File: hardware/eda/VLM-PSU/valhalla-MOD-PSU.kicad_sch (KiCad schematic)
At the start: 58 parts, among them J1 MAINS, J2 DC, J3 BUS, J4 GPIO, J5 POWER, Q1 BTA08-600CW, Q10 IRF9Z34N, Q2 2N3904, Q3 2N3906, Q4 2N3906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

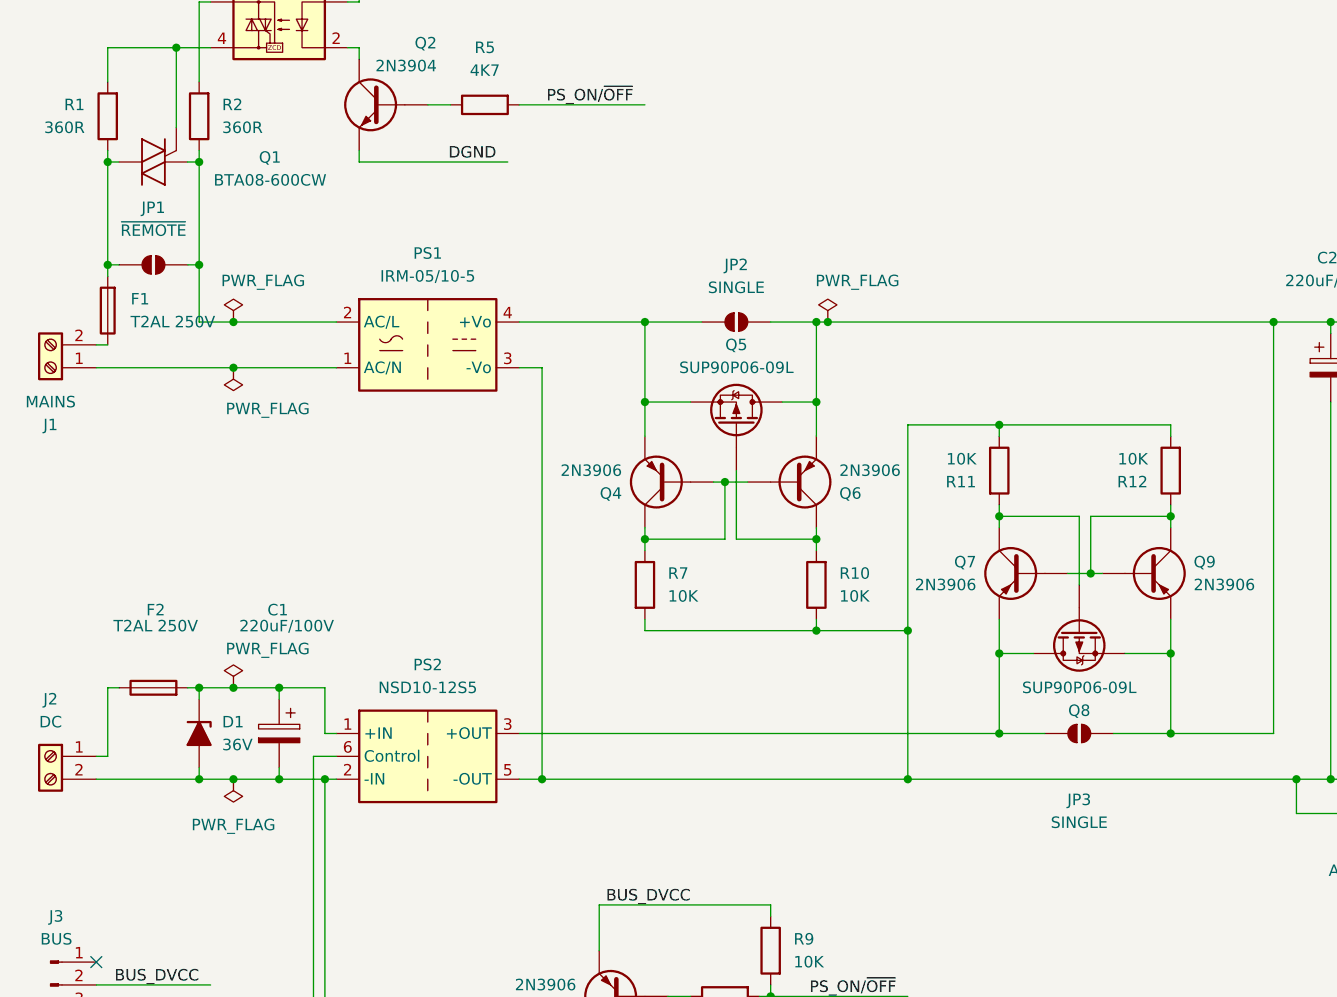
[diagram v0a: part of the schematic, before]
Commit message: UPDATE: tentative component placement for MOD-PSU
  - everything fits with room to spare
  - clearance/creepage for the mains section appears fine
  - zones/slots are next.
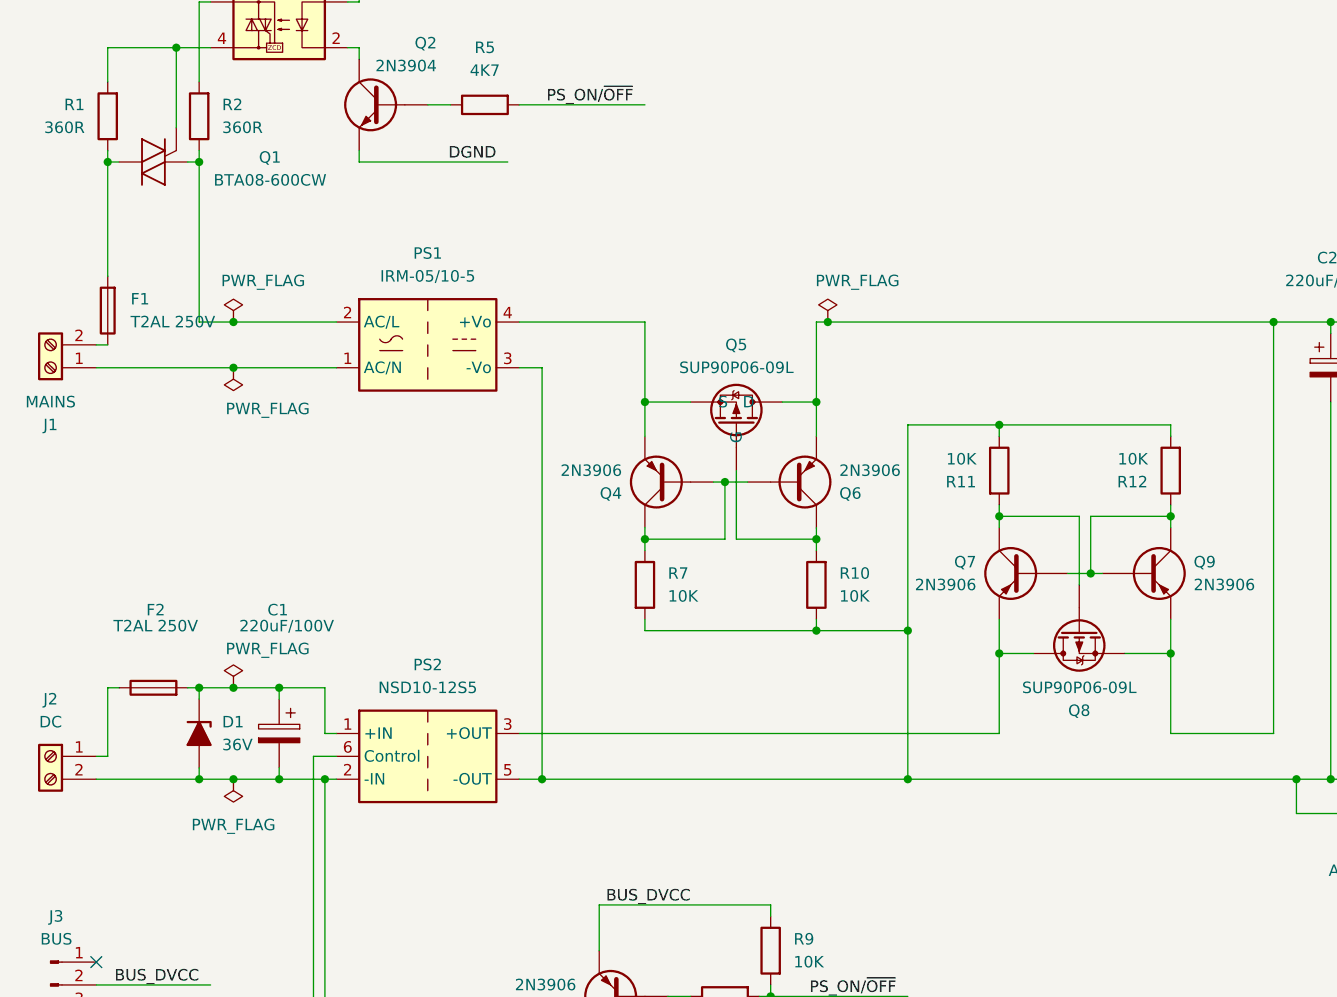
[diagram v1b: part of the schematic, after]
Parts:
- removed JP1: ~{REMOTE}, Jumper:SolderJumper-2_P1.3mm_Open_TrianglePad1.0x1.5mm, symbol Jumper:SolderJumper_2_Open
- removed JP2, JP3: SINGLE, Jumper:SolderJumper-2_P1.3mm_Open_TrianglePad1.0x1.5mm, symbol Jumper:SolderJumper_2_Open
- U3: footprint Package_TO_SOT_THT:TO-92_Inline -> Package_TO_SOT_THT:TO-92_Wide

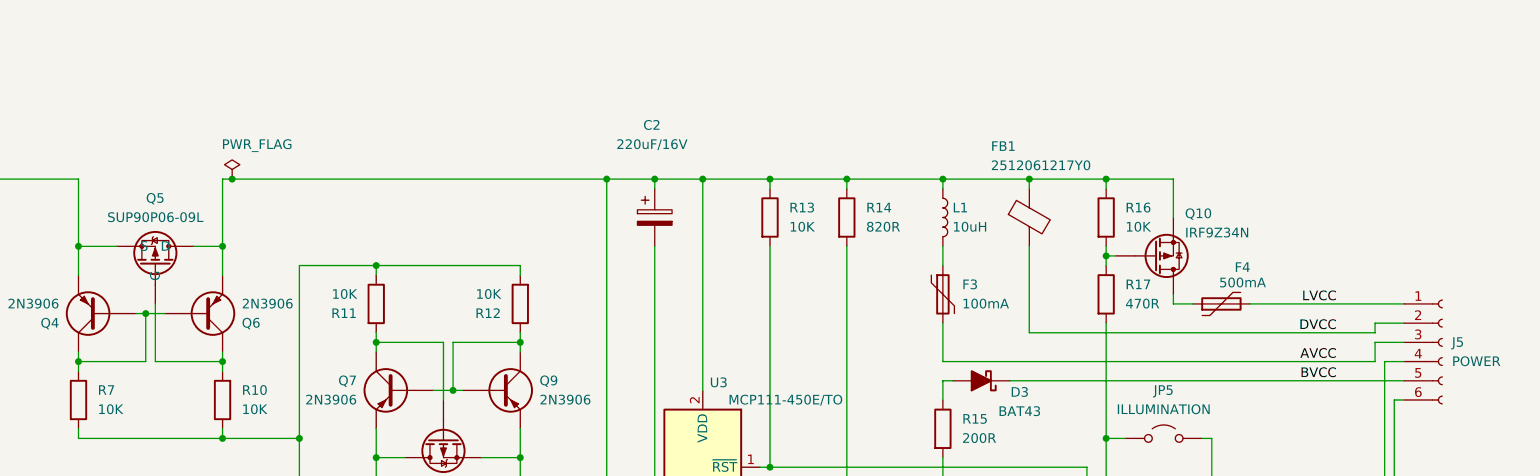
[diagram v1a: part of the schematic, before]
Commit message: UPDATE: progress on MOD-PSU layout
  - zones and slots done
  - heatsink pours and stiches done
  - routing is next.
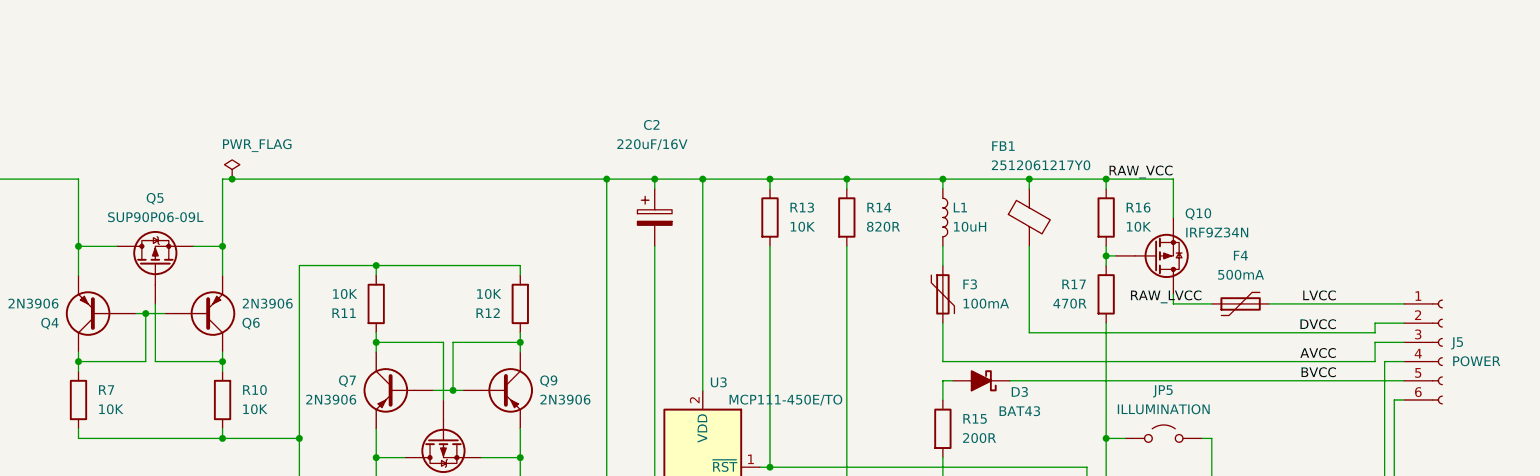
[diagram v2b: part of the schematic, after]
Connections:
- net RAW_LVCC: now reaches F4.1, Q10.2 (D)
- net RAW_VCC: now reaches C2.1, FB1.1, L1.1, Q10.3 (S), Q6.1 (E), Q8.3 (S), Q9.1 (E), R13.1, R14.1, R16.1, U3.2 (VDD)
- net RAW_VCC: now also Q5.3 (S); no longer Q5.2 (D)
- net at PS1.4 (+Vo), Q4.1 (E): now also Q5.2 (D); no longer Q5.3 (S)
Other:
- moved on the sheet: F4
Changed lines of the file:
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@@
 	(wire
 		(pts
-			(xy 228.6 78.74) (xy 231.14 78.74)
+			(xy 228.6 78.74) (xy 233.68 78.74)
 		)
 		(stroke
@@
 	(wire
 		(pts
-			(xy 238.76 78.74) (xy 259.08 78.74)
+			(xy 241.3 78.74) (xy 259.08 78.74)
 		)
 		(stroke
@@
 		)
 	)
+	(label "RAW_VCC"
+		(at 228.6 62.23 180)
+		(effects
+			(font
+				(size 1.27 1.27)
+			)
+			(justify right bottom)
+		)
+	)
 	(label "DGND"
 		(at 250.19 113.03 180)
@@
 		)
 	)
+	(label "RAW_LVCC"
+		(at 232.41 78.74 180)
+		(effects
+			(font
+				(size 1.27 1.27)
+			)
+			(justify right bottom)
+		)
+	)
 	(label "PS_ON{slash}~{OFF}"
 		(at 111.76 137.16 180)
@@
 		(fields_autoplaced yes)
 		(property "Reference" "R17"
-			(at 222.25 76.1999 0)
+			(at 217.17 76.1999 0)
 			(effects
 				(font
 					(size 1.27 1.27)
 				)
-				(justify left)
+				(justify right)
 			)
 		)
 		(property "Value" "470R"
-			(at 222.25 78.7399 0)
+			(at 217.17 78.7399 0)
 			(effects
 				(font
 					(size 1.27 1.27)
 				)
-				(justify left)
+				(justify right)
 			)
 		)
@@
 		(lib_name "IRF4905_2")
 		(lib_id "Transistor_FET:IRF4905")
-		(at 93.98 73.66 270)
-		(mirror x)
+		(at 93.98 73.66 90)
 		(unit 1)
 		(exclude_from_sim no)
@@
 		)
 		(property "Footprint" "Package_TO_SOT_THT:TO-220-3_Horizontal_TabDown"
-			(at 92.075 68.58 0)
+			(at 95.885 68.58 0)
 			(effects
 				(font
@@
 		)
 		(property "Datasheet" "http://www.infineon.com/dgdl/irf4905.pdf?fileId=5546d462533600a4015355e32165197c"
-			(at 90.17 68.58 0)
+			(at 97.79 68.58 0)
 			(effects
 				(font
@@
 	(symbol
 		(lib_id "Device:Polyfuse")
-		(at 234.95 78.74 90)
+		(at 237.49 78.74 90)
 		(unit 1)
 		(exclude_from_sim no)
@@
 		(on_board yes)
 		(dnp no)
+		(fields_autoplaced yes)
 		(property "Reference" "F4"
-			(at 237.744 73.914 90)
+			(at 237.49 72.39 90)
 			(effects
 				(font
@@
 		)
 		(property "Value" "500mA"
-			(at 237.744 75.946 90)
+			(at 237.49 74.93 90)
 			(effects
 				(font
@@
 		)
 		(property "Footprint" "Fuse:Fuse_BelFuse_0ZRE0005FF_L8.3mm_W3.8mm"
-			(at 240.03 77.47 0)
+			(at 242.57 77.47 0)
 			(effects
 				(font
@@
 		)
 		(property "Datasheet" "~"
-			(at 234.95 78.74 0)
+			(at 237.49 78.74 0)
 			(effects
 				(font
@@
 		)
 		(property "Description" "Resettable fuse, polymeric positive temperature coefficient"
-			(at 234.95 78.74 0)
+			(at 237.49 78.74 0)
 			(effects
 				(font

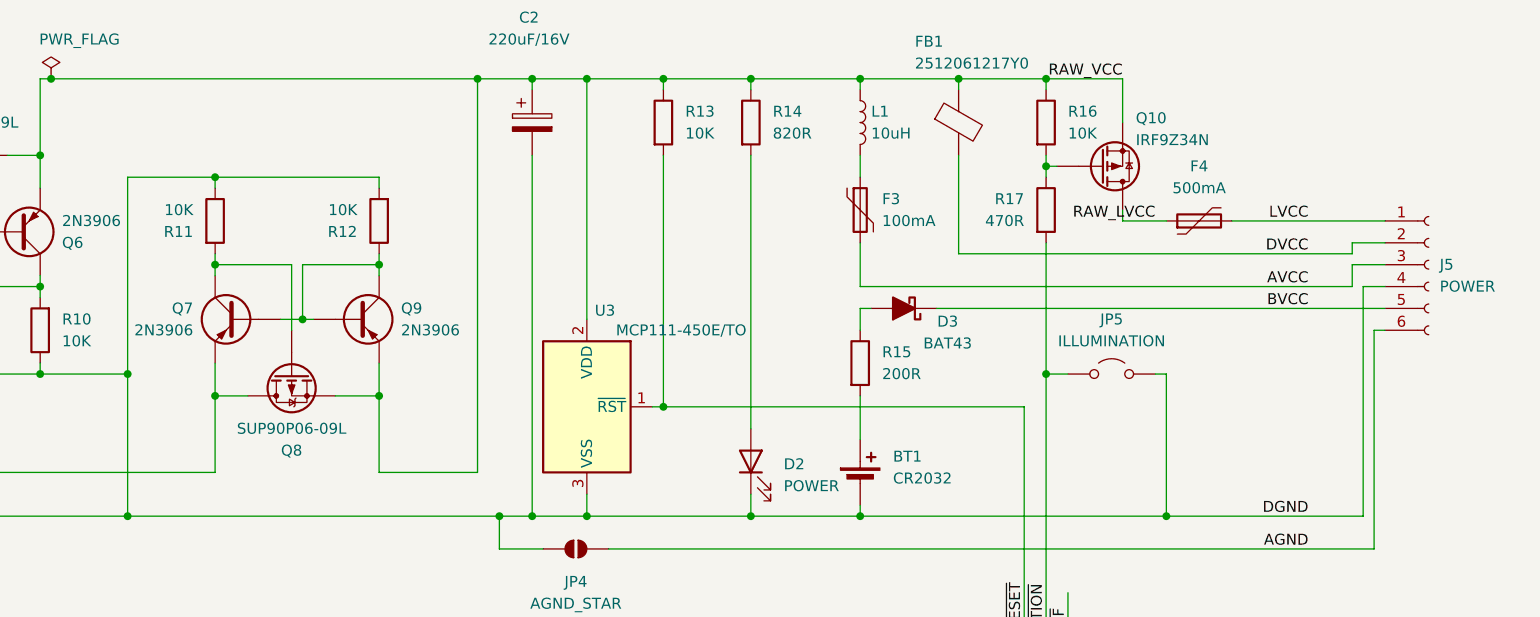
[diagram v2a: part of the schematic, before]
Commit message: UPDATE: progress on MOD-PSU
  - routing done, including copper heatsinks
  - silkscreen is last.
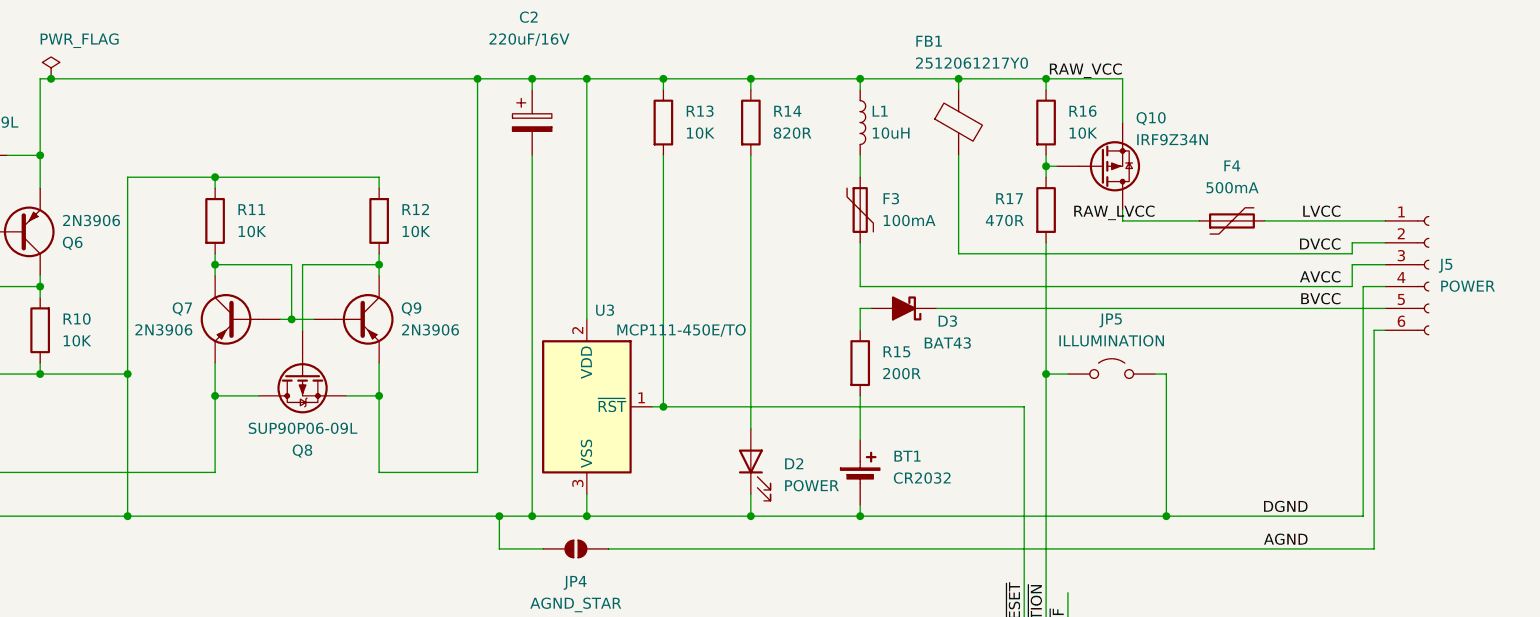
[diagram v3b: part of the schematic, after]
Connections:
- net at Q7.2 (B), Q9.2 (B): now also Q7.3 (C), R11.2; no longer Q9.3 (C), R12.1
- new net: Q8.1 (G), Q9.3 (C), R12.1
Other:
- moved on the sheet: F4, Q8
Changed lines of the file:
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@@
 	)
 	(junction
-		(at 133.35 90.17)
-		(diameter 0)
-		(color 0 0 0 0)
-	)
-	(junction
 		(at 219.71 62.23)
 		(diameter 0)
@@
 	)
 	(junction
+		(at 132.08 90.17)
+		(diameter 0)
+		(color 0 0 0 0)
+	)
+	(junction
 		(at 123.19 99.06)
 		(diameter 0)
@@
 	(wire
 		(pts
-			(xy 228.6 78.74) (xy 233.68 78.74)
+			(xy 228.6 78.74) (xy 237.49 78.74)
 		)
 		(stroke
@@
 	(wire
 		(pts
-			(xy 241.3 78.74) (xy 259.08 78.74)
+			(xy 245.11 78.74) (xy 259.08 78.74)
 		)
 		(stroke
@@
 	(wire
 		(pts
+			(xy 132.08 90.17) (xy 134.62 90.17)
+		)
+		(stroke
+			(width 0)
+			(type default)
+		)
+	)
+	(wire
+		(pts
 			(xy 219.71 72.39) (xy 220.98 72.39)
 		)
@@
 	(wire
 		(pts
+			(xy 133.35 83.82) (xy 133.35 91.44)
+		)
+		(stroke
+			(width 0)
+			(type default)
+		)
+	)
+	(wire
+		(pts
 			(xy 34.29 113.03) (xy 38.1 113.03)
 		)
@@
 	(wire
 		(pts
-			(xy 130.81 90.17) (xy 133.35 90.17)
+			(xy 130.81 90.17) (xy 132.08 90.17)
 		)
 		(stroke
@@
 	(wire
 		(pts
-			(xy 132.08 91.44) (xy 132.08 83.82)
-		)
-		(stroke
-			(width 0)
-			(type default)
-		)
-	)
-	(wire
-		(pts
 			(xy 24.13 31.75) (xy 31.75 31.75)
 		)
@@
 	(wire
 		(pts
-			(xy 137.16 99.06) (xy 142.24 99.06)
+			(xy 138.43 99.06) (xy 142.24 99.06)
 		)
 		(stroke
@@
 	(wire
 		(pts
+			(xy 132.08 83.82) (xy 132.08 90.17)
+		)
+		(stroke
+			(width 0)
+			(type default)
+		)
+	)
+	(wire
+		(pts
 			(xy 142.24 83.82) (xy 133.35 83.82)
 		)
@@
 	(wire
 		(pts
-			(xy 127 99.06) (xy 123.19 99.06)
+			(xy 128.27 99.06) (xy 123.19 99.06)
 		)
 		(stroke
@@
 	(wire
 		(pts
-			(xy 133.35 90.17) (xy 134.62 90.17)
-		)
-		(stroke
-			(width 0)
-			(type default)
-		)
-	)
-	(wire
-		(pts
 			(xy 62.23 156.21) (xy 46.99 156.21)
 		)
@@
 	(wire
 		(pts
-			(xy 133.35 83.82) (xy 133.35 90.17)
-		)
-		(stroke
-			(width 0)
-			(type default)
-		)
-	)
-	(wire
-		(pts
 			(xy 256.54 86.36) (xy 256.54 113.03)
 		)
@@
 	)
 	(label "AVCC"
-		(at 250.19 86.36 180)
+		(at 254 86.36 180)
 		(effects
 			(font
@@
 	)
 	(label "LVCC"
-		(at 250.19 78.74 180)
+		(at 254 78.74 180)
 		(effects
 			(font
@@
 	)
 	(label "DVCC"
-		(at 250.19 82.55 180)
+		(at 254 82.55 180)
 		(effects
 			(font
@@
 	)
 	(label "BVCC"
-		(at 250.19 88.9 180)
+		(at 254 88.9 180)
 		(effects
 			(font
@@
 		(length 2.54)
 		(shape round)
+		(at 228.6 78.74 180)
+		(fields_autoplaced yes)
+		(effects
+			(font
+				(size 1.27 1.27)
+			)
+			(justify right bottom)
+		)
+		(property "Netclass" "DCD_Power"
+			(at 229.2985 81.28 0)
+			(effects
+				(font
+					(size 1.27 1.27)
+					(italic yes)
+				)
+				(justify left)
+			)
+		)
+	)
+	(netclass_flag ""
+		(length 2.54)
+		(shape round)
 		(at 24.13 67.31 180)
 		(fields_autoplaced yes)
@@
 		(length 2.54)
 		(shape round)
-		(at 242.57 86.36 0)
+		(at 246.38 86.36 0)
 		(fields_autoplaced yes)
 		(effects
@@
 		)
 		(property "Netclass" "DCA_Power"
-			(at 243.2685 83.82 0)
+			(at 247.0785 83.82 0)
 			(effects
 				(font
@@
 		(length 2.54)
 		(shape round)
-		(at 242.57 82.55 0)
+		(at 246.38 82.55 0)
 		(fields_autoplaced yes)
 		(effects
@@
 		)
 		(property "Netclass" "DCD_Power"
-			(at 243.2685 80.01 0)
+			(at 247.0785 80.01 0)
 			(effects
 				(font
@@
 		(length 2.54)
 		(shape round)
-		(at 242.57 78.74 0)
+		(at 246.38 78.74 0)
 		(fields_autoplaced yes)
 		(effects
@@
 		)
 		(property "Netclass" "DCD_Power"
-			(at 243.2685 76.2 0)
+			(at 247.0785 76.2 0)
 			(effects
 				(font
@@
 		(lib_name "IRF4905_1")
 		(lib_id "Transistor_FET:IRF4905")
-		(at 132.08 96.52 90)
+		(at 133.35 96.52 90)
 		(mirror x)
 		(unit 1)
@@
 		(dnp no)
 		(property "Reference" "Q8"
-			(at 132.08 105.41 90)
+			(at 133.35 105.41 90)
 			(effects
 				(font
@@
 		)
 		(property "Value" "SUP90P06-09L"
-			(at 132.08 102.87 90)
+			(at 133.35 102.87 90)
 			(effects
 				(font
@@
 		)
 		(property "Footprint" "Package_TO_SOT_THT:TO-220-3_Horizontal_TabDown"
-			(at 133.985 101.6 0)
+			(at 135.255 101.6 0)
 			(effects
 				(font
@@
 		)
 		(property "Datasheet" "http://www.infineon.com/dgdl/irf4905.pdf?fileId=5546d462533600a4015355e32165197c"
-			(at 135.89 101.6 0)
+			(at 137.16 101.6 0)
 			(effects
 				(font
@@
 		)
 		(property "Description" "-74A Id, -55V Vds, Single P-Channel HEXFET Power MOSFET, 20mOhm Ron, TO-220AB"
-			(at 132.08 96.52 0)
+			(at 133.35 96.52 0)
 			(effects
 				(font
@@
 		(fields_autoplaced yes)
 		(property "Reference" "R12"
-			(at 139.7 80.0101 0)
+			(at 144.78 77.4699 0)
 			(effects
 				(font
 					(size 1.27 1.27)
 				)
-				(justify left)
+				(justify right)
 			)
 		)
 		(property "Value" "10K"
-			(at 139.7 77.4701 0)
+			(at 144.78 80.0099 0)
 			(effects
 				(font
 					(size 1.27 1.27)
 				)
-				(justify left)
+				(justify right)
 			)
 		)
@@
 		(fields_autoplaced yes)
 		(property "Reference" "R11"
-			(at 120.65 80.0101 0)
+			(at 125.73 77.4699 0)
 			(effects
 				(font
 					(size 1.27 1.27)
 				)
-				(justify right)
+				(justify left)
 			)
 		)
 		(property "Value" "10K"
-			(at 120.65 77.4701 0)
+			(at 125.73 80.0099 0)
 			(effects
 				(font
 					(size 1.27 1.27)
 				)
-				(justify right)
+				(justify left)
 			)
 		)
@@
 	(symbol
 		(lib_id "Device:Polyfuse")
-		(at 237.49 78.74 90)
+		(at 241.3 78.74 90)
 		(unit 1)
 		(exclude_from_sim no)
@@
 		(fields_autoplaced yes)
 		(property "Reference" "F4"
-			(at 237.49 72.39 90)
+			(at 241.3 72.39 90)
 			(effects
 				(font
@@
 		)
 		(property "Value" "500mA"
-			(at 237.49 74.93 90)
+			(at 241.3 74.93 90)
 			(effects
 				(font
@@
 		)
 		(property "Footprint" "Fuse:Fuse_BelFuse_0ZRE0005FF_L8.3mm_W3.8mm"
-			(at 242.57 77.47 0)
+			(at 246.38 77.47 0)
 			(effects
 				(font
@@
 		)
 		(property "Datasheet" "~"
-			(at 237.49 78.74 0)
+			(at 241.3 78.74 0)
 			(effects
 				(font
@@
 		)
 		(property "Description" "Resettable fuse, polymeric positive temperature coefficient"
-			(at 237.49 78.74 0)
+			(at 241.3 78.74 0)
 			(effects
 				(font
